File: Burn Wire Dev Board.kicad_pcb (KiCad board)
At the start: 2 copper layers, 77 x 20 mm, 41 parts, among them J1 282834-2, J2 J-TSM-106-01-F-SV, J3 J-0532610671, SW1 FSMSM, U2 ADP2303ARDZ

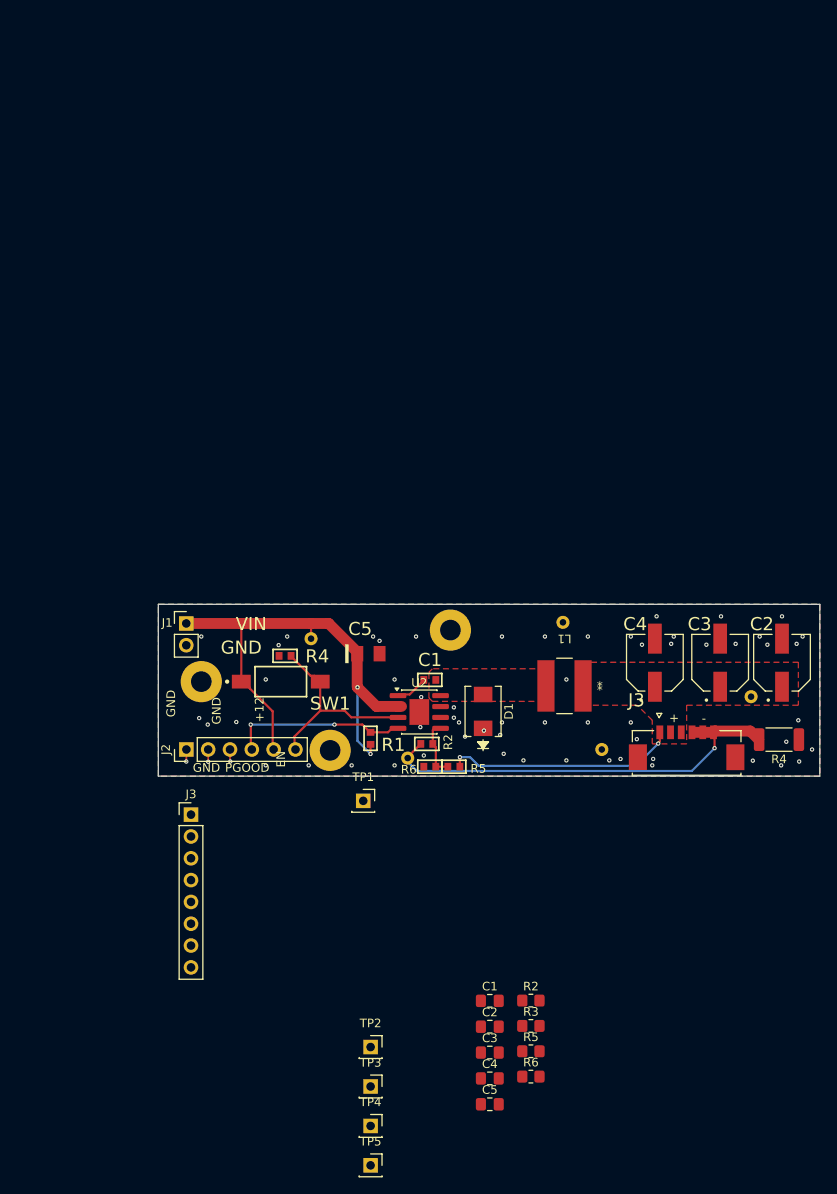
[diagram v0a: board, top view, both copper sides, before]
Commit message: added compute resistor tolayout
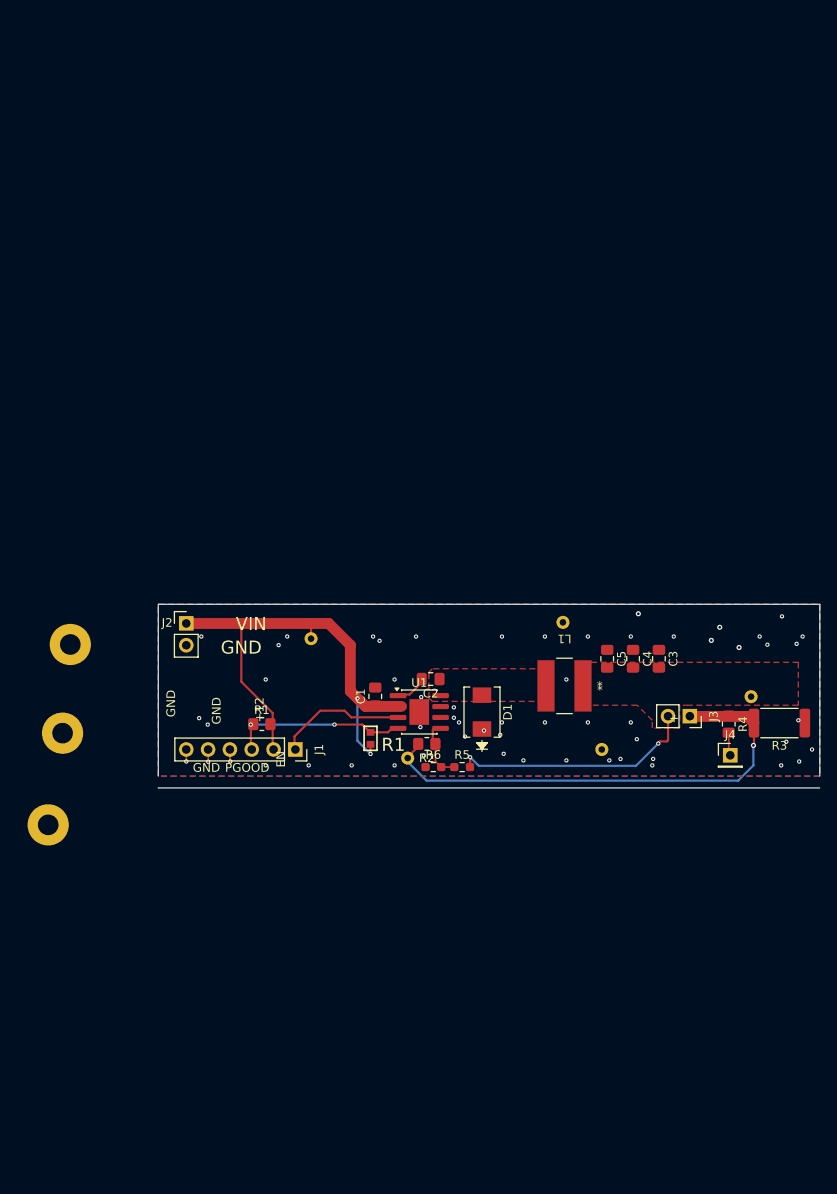
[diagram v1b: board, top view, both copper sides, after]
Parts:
- removed the C1 at (141.6, 103.8)
- removed the C2 at (182.6, 101.8)
- removed the C3 at (175.4, 101.8)
- removed the C4 at (167.8, 101.8)
- removed the C5 at (134.5, 100.8)
- removed the J2 at (113.3, 111.9)
- removed the J3 at (171.5, 112.3)
- removed the J3 at (113.8, 119.5)
- removed the R2 at (141.3, 111.3)
- removed the R4 at (182.3, 110.8)
- removed the R4 at (124.8, 101.0)
- removed the R5 at (153.4, 147.0)
- removed the R5 at (144.4, 113.9)
- removed the R6 at (153.4, 150.0)
- removed the R6 at (141.6, 113.9)
- removed SW1: FSMSM, Vault:TECO-FSMSM-2_V
- removed the TP1 at (133.9, 117.9)
- removed the TP2 at (134.7, 146.5)
- removed the TP3 at (134.7, 151.1)
- removed the TP4 at (134.7, 155.7)
- removed the TP5 at (134.7, 160.3)
- added J1: Conn_01x06_Pin, Connector_PinSocket_2.54mm:PinSocket_1x06_P2.54mm_Vertical, F.Cu at (126.0, 111.9)
- added J3: Conn_01x02_Pin, Connector_PinSocket_2.54mm:PinSocket_1x02_P2.54mm_Vertical, F.Cu at (171.9, 108.0)
- added J4: Conn_01x01_Pin, Connector_PinHeader_2.54mm:PinHeader_1x01_P2.54mm_Vertical, F.Cu at (176.6, 112.6)
- added R3: 0.25R, Resistor_SMD:R_2512_6332Metric, F.Cu at (182.3, 108.8)
- added R4: 1k, Resistor_SMD:R_0805_2012Metric_Pad1.20x1.40mm_HandSolder, F.Cu at (176.4, 109.0)
- added R5: 0R, Resistor_SMD:R_0603_1608Metric_Pad0.98x0.95mm_HandSolder, F.Cu at (145.4, 114.0)
- added R6: 0R, Resistor_SMD:R_0603_1608Metric_Pad0.98x0.95mm_HandSolder, F.Cu at (142.0, 114.0)
- D1: value B540C-13-F -> D_Schottky
- moved C5 53.6 mm to (162.3, 101.3), turned to -90 degrees
- moved C4 51.6 mm to (165.3, 101.3), turned to -90 degrees
- moved C3 49.9 mm to (168.3, 101.3), turned to -90 degrees
- moved R1 44.9 mm to (122.1, 109.0)
- moved *1 44.3 mm to (99.8, 99.7)
- moved C2 41.1 mm to (141.7, 103.7), turned to 180 degrees
- moved C1 37.9 mm to (135.3, 105.7), turned to 90 degrees
- moved R2 35.0 mm to (141.3, 111.3), turned to 180 degrees
- moved *3 34.0 mm to (97.2, 120.7)
- moved *2 17.2 mm to (98.9, 110.0)
- moved D1 0.15 mm to (147.7, 107.6)
- renumbered J1 to J2, R2 to R1, R3 to R2, U2 to U1
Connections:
- net +5 renamed +VBATT
- C2 pad 1: Net-(U2-SW) -> Net-(D1-A)
- D1 pad 1: (no net) -> GND
- D1 pad 2: (no net) -> Net-(D1-A)
- L1 pad 2: Net-(U2-SW) -> Net-(D1-A)
- TP1 pad 1: BURN_POS -> /BURN_POS
- TP3 pad 1: BURN_NEG -> /BURN_NEG
- U1 pad 8: Net-(U2-SW) -> Net-(D1-A)
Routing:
- net /BURN_NEG: track 0.00 -> 57.4 mm, vias 0 -> 1
- net BURN_NEG: track 49.8 -> 0.00 mm, vias 1 -> 0
- net /BURN_POS: track 0.00 -> 28.7 mm, vias 0 -> 2
- net BURN_POS: track 27.1 -> 0.00 mm, vias 2 -> 0
- net ENABLE: track 22.7 -> 0.00 mm
- net /ENABLE: track 0.00 -> 14.7 mm
- net Net-(U1-FB): track 0.00 -> 7.64 mm
- net NetR2_1: track 6.79 -> 0.00 mm
- net NetC1_2: track 3.79 -> 0.00 mm
- net Net-(U1-BST): track 0.00 -> 3.79 mm
- net TO_COMPUTE: track 0.00 -> 2.70 mm
- net +VBATT: track 59.1 -> 58.4 mm
- net GND: vias 56 -> 58
- net (no net): vias 6 -> 0
- added copper zone on F.Cu, net /BURN_POS
- added copper zone on F.Cu, net Net-(D1-A)
- removed copper zone on F.Cu, net BURN_POS
- removed copper zone on F.Cu, net Net-(U2-SW)
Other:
- board size 77 x 20 mm -> 77 x 21.4 mm
- board text removed: "-"

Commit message: done
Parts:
- removed the *3 at (97.2, 120.7)
- added *3: M2 Mounting, PowerManagmentBoard_V4.0:M2 Screws, F.Cu at (106.3, 31.7)
- added *3: M2 Mounting, PowerManagmentBoard_V4.0:M2 Screws, F.Cu at (175.0, 31.7)
- moved *2 80.7 mm to (175.0, 136.7)
- moved *1 37.6 mm to (106.3, 136.7)
- moved L1 8.66 mm to (148.6, 104.1)
- moved C5 7.95 mm to (154.3, 101.1)
- moved J3 7.95 mm to (163.9, 107.7)
- moved R2 7.95 mm to (133.3, 111.0)
- moved R4 7.95 mm to (168.5, 108.7)
- moved TP3 7.95 mm to (131.1, 112.6)
- moved TP4 7.95 mm to (149.1, 96.8)
- moved U1 7.95 mm to (132.4, 107.3)
- moved C1 7.95 mm to (127.3, 105.4)
- moved J1 7.95 mm to (118.0, 111.6)
- moved R1 7.95 mm to (126.8, 110.3)
- moved R1 7.95 mm to (114.1, 108.7)
- moved C2 7.95 mm to (133.8, 103.4)
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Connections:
- *2 pad 1: GND -> (no net)
- J1 pad 3: /PGOOD -> PGOOD
- R1 pad 1: /PGOOD -> PGOOD
- U1 pad 4: /PGOOD -> PGOOD
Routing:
- net /BURN_POS: track 28.7 -> 37.1 mm
- net GND: vias 58 -> 57
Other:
- board size 77 x 21.4 mm -> 92.2 x 41.8 mm

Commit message: fixed physical dim to have edgecuts
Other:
- board size 92.2 x 41.8 mm -> 82.8 x 115 mm
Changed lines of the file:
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@@
 		(sheetname "/")
 		(sheetfile "Burn Wire Dev Board.kicad_sch")
-		(units
-			(unit
-				(name "A")
-				(pins "1" "2")
-			)
-		)
 		(attr smd)
 		(duplicate_pad_numbers_are_jumpers no)
@@
 		(sheetname "/")
 		(sheetfile "Burn Wire Dev Board.kicad_sch")
-		(units
-			(unit
-				(name "A")
-				(pins "1" "2")
-			)
-		)
 		(attr smd)
 		(duplicate_pad_numbers_are_jumpers no)
@@
 		(sheetname "/")
 		(sheetfile "Burn Wire Dev Board.kicad_sch")
-		(units
-			(unit
-				(name "A")
-				(pins "1" "2")
-			)
-		)
 		(attr smd)
 		(duplicate_pad_numbers_are_jumpers no)
@@
 		)
 		(embedded_fonts no)
-		(embedded_files)
 		(model "kicad-embed://92000A011_Passivated 18-8 Stainless Steel Pan Head Phillips Screws.STEP"
 			(offset
@@
 		(sheetname "/")
 		(sheetfile "Burn Wire Dev Board.kicad_sch")
-		(units
-			(unit
-				(name "A")
-				(pins "1" "2")
-			)
-		)
 		(attr smd)
 		(duplicate_pad_numbers_are_jumpers no)
@@
 		(sheetname "/")
 		(sheetfile "Burn Wire Dev Board.kicad_sch")
-		(units
-			(unit
-				(name "A")
-				(pins "1")
-			)
-		)
 		(attr through_hole)
 		(duplicate_pad_numbers_are_jumpers no)
@@
 			(pinfunction "Pin_1_1")
 			(pintype "passive")
-			(solder_mask_margin 0.2)
-			(solder_paste_margin 0)
-			(clearance 0.2)
 		)
 		(embedded_fonts no)
@@
 		(sheetname "/")
 		(sheetfile "Burn Wire Dev Board.kicad_sch")
-		(units
-			(unit
-				(name "A")
-				(pins "1" "2" "3" "4" "5" "6")
-			)
-		)
 		(attr through_hole)
 		(duplicate_pad_numbers_are_jumpers no)
@@
 		(sheetname "/")
 		(sheetfile "Burn Wire Dev Board.kicad_sch")
-		(units
-			(unit
-				(name "A")
-				(pins "2" "3" "4" "6" "7" "9" "1" "8" "5")
-			)
-		)
 		(attr smd)
 		(duplicate_pad_numbers_are_jumpers no)
@@
 		(sheetname "/")
 		(sheetfile "Burn Wire Dev Board.kicad_sch")
-		(units
-			(unit
-				(name "A")
-				(pins "1" "2")
-			)
-		)
 		(attr through_hole)
 		(duplicate_pad_numbers_are_jumpers no)
@@
 		(sheetname "/")
 		(sheetfile "Burn Wire Dev Board.kicad_sch")
-		(units
-			(unit
-				(name "A")
-				(pins "2" "1")
-			)
-		)
 		(attr through_hole)
 		(duplicate_pad_numbers_are_jumpers no)
@@
 		)
 		(embedded_fonts no)
-		(embedded_files)
 		(model "kicad-embed://92000A011_Passivated 18-8 Stainless Steel Pan Head Phillips Screws.STEP"
 			(offset
@@
 		(sheetname "/")
 		(sheetfile "Burn Wire Dev Board.kicad_sch")
-		(units
-			(unit
-				(name "A")
-				(pins "1" "2")
-			)
-		)
 		(attr smd)
 		(duplicate_pad_numbers_are_jumpers no)
@@
 		(sheetname "/")
 		(sheetfile "Burn Wire Dev Board.kicad_sch")
-		(units
-			(unit
-				(name "A")
-				(pins "1" "2")
-			)
-		)
 		(attr smd)
 		(duplicate_pad_numbers_are_jumpers no)
@@
 		)
 		(embedded_fonts no)
-		(embedded_files)
 		(model "kicad-embed://92000A011_Passivated 18-8 Stainless Steel Pan Head Phillips Screws.STEP"
 			(offset
@@
 		(sheetname "/")
 		(sheetfile "Burn Wire Dev Board.kicad_sch")
-		(units
-			(unit
-				(name "A")
-				(pins "1" "2")
-			)
-		)
 		(attr smd)
 		(duplicate_pad_numbers_are_jumpers no)
@@
 		(sheetname "/")
 		(sheetfile "Burn Wire Dev Board.kicad_sch")
-		(units
-			(unit
-				(name "A")
-				(pins "1" "2")
-			)
-		)
 		(attr smd)
 		(duplicate_pad_numbers_are_jumpers no)
@@
 			(pintype "passive")
 		)
-		(variant
-			(name "Build")
-			(dnp yes)
-			(exclude_from_bom yes)
-			(exclude_from_pos_files yes)
-		)
 		(embedded_fonts no)
 		(model "${KICAD10_3DMODEL_DIR}/Resistor_SMD.3dshapes/R_0603_1608Metric.step"
@@
 		(sheetname "/")
 		(sheetfile "Burn Wire Dev Board.kicad_sch")
-		(units
-			(unit
-				(name "A")
-				(pins "1" "2")
-			)
-		)
 		(attr smd)
 		(duplicate_pad_numbers_are_jumpers no)
@@
 			(pintype "passive")
 		)
-		(variant
-			(name "Build")
-			(dnp yes)
-			(exclude_from_bom yes)
-			(exclude_from_pos_files yes)
-		)
 		(embedded_fonts no)
 		(model "${KICAD10_3DMODEL_DIR}/Resistor_SMD.3dshapes/R_0603_1608Metric.step"
@@
 		(sheetname "/")
 		(sheetfile "Burn Wire Dev Board.kicad_sch")
-		(units
-			(unit
-				(name "A")
-				(pins "1" "2")
-			)
-		)
 		(attr smd)
 		(duplicate_pad_numbers_are_jumpers no)
@@
 			(pintype "passive")
 		)
-		(variant
-			(name "Build")
-			(dnp yes)
-			(exclude_from_bom yes)
-			(exclude_from_pos_files yes)
-		)
 		(embedded_fonts no)
 		(model "${KICAD10_3DMODEL_DIR}/Resistor_SMD.3dshapes/R_2512_6332Metric.step"
@@
 		(sheetname "/")
 		(sheetfile "Burn Wire Dev Board.kicad_sch")
-		(units
-			(unit
-				(name "A")
-				(pins "1" "2")
-			)
-		)
 		(attr smd)
 		(duplicate_pad_numbers_are_jumpers no)
@@
 	)
 	(gr_rect
-		(start 93.5911 84.46845)
-		(end 185.8311 126.23875)
+		(start 99.2645 26.7032)
+		(end 182.0177 141.6636)
 		(stroke
-			(width 0.05)
+			(width 0.1)
 			(type solid)
 		)
